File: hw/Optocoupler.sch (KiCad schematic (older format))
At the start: 10 parts, among them J1 Conn_01x02_Female, U2 EL357N(A)(TA)-G

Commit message: Add connectors
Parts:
- gave numbers to parts that had none: 6
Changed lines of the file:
@@
 $EndComp
 $Comp
-L Device:R R?
+L Device:R R7
 U 1 1 5F8C6DD6
 P 7100 2500
-F 0 "R?" H 7170 2546 50  0000 L CNN
+F 0 "R7" H 7170 2546 50  0000 L CNN
 F 1 "10k" H 7170 2455 50  0000 L CNN
 F 2 "" V 7030 2500 50  0001 C CNN
@@
 	7100 2950 7100 3050
 $Comp
-L power:GND #PWR?
+L power:GND #PWR0109
 U 1 1 5F8C950C
 P 7100 3050
-F 0 "#PWR?" H 7100 2800 50  0001 C CNN
+F 0 "#PWR0109" H 7100 2800 50  0001 C CNN
 F 1 "GND" H 7105 2877 50  0000 C CNN
 F 2 "" H 7100 3050 50  0001 C CNN
@@
 P 6300 4550
 AR Path="/5F8D198E" Ref="U?"  Part="1"
-AR Path="/5F8B0B95/5F8D198E" Ref="U?"  Part="1"
-F 0 "U?" H 6300 4920 50  0000 C CNN
+AR Path="/5F8B0B95/5F8D198E" Ref="U1"  Part="1"
+F 0 "U1" H 6300 4920 50  0000 C CNN
 F 1 "EL357N(A)(TA)-G" H 6300 4829 50  0000 C CNN
 F 2 "EL357N_A__TA_-G:SOP254P700X200-4N" H 6300 4550 50  0001 L BNN
@@
 $EndComp
 $Comp
-L Connector:Conn_01x02_Female J?
+L Connector:Conn_01x02_Female J2
 U 1 1 5F8D1994
 P 4100 4600
-F 0 "J?" H 3992 4275 50  0000 C CNN
+F 0 "J2" H 3992 4275 50  0000 C CNN
 F 1 "Conn_01x02_Female" H 3992 4366 50  0000 C CNN
 F 2 "" H 4100 4600 50  0001 C CNN
@@
 $EndComp
 $Comp
-L B5819W:B5819W D?
+L B5819W:B5819W D3
 U 1 1 5F8D199A
 P 5300 4550
-F 0 "D?" V 5346 4460 50  0000 R CNN
+F 0 "D3" V 5346 4460 50  0000 R CNN
 F 1 "B5819W" V 5255 4460 50  0000 R CNN
 F 2 "B5819W:B5819W_SOD-123" H 5300 4550 50  0001 L BNN
@@
 	4850 4500 5000 4500
 $Comp
-L Device:R R?
+L Device:R R6
 U 1 1 5F8D19AB
 P 4700 4500
-F 0 "R?" V 4493 4500 50  0000 C CNN
+F 0 "R6" V 4493 4500 50  0000 C CNN
 F 1 "20k" V 4584 4500 50  0000 C CNN
 F 2 "" V 4630 4500 50  0001 C CNN
@@
 $EndComp
 $Comp
-L Device:R R?
+L Device:R R8
 U 1 1 5F8D19B1
 P 7100 4200
-F 0 "R?" H 7170 4246 50  0000 L CNN
+F 0 "R8" H 7170 4246 50  0000 L CNN
 F 1 "10k" H 7170 4155 50  0000 L CNN
 F 2 "" V 7030 4200 50  0001 C CNN
@@
 	7100 4650 7100 4750
 $Comp
-L power:GND #PWR?
+L power:GND #PWR0110
 U 1 1 5F8D19BD
 P 7100 4750
-F 0 "#PWR?" H 7100 4500 50  0001 C CNN
+F 0 "#PWR0110" H 7100 4500 50  0001 C CNN
 F 1 "GND" H 7105 4577 50  0000 C CNN
 F 2 "" H 7100 4750 50  0001 C CNN
@@
 OPTO_STOP
 $Comp
-L power:+3V3 #PWR?
+L power:+3V3 #PWR0111
 U 1 1 5F8E1D5E
 P 7100 4050
-F 0 "#PWR?" H 7100 3900 50  0001 C CNN
+F 0 "#PWR0111" H 7100 3900 50  0001 C CNN
 F 1 "+3V3" H 7115 4223 50  0000 C CNN
 F 2 "" H 7100 4050 50  0001 C CNN
@@
 $EndComp
 $Comp
-L power:+3V3 #PWR?
+L power:+3V3 #PWR0112
 U 1 1 5F8E5015
 P 7100 2350
-F 0 "#PWR?" H 7100 2200 50  0001 C CNN
+F 0 "#PWR0112" H 7100 2200 50  0001 C CNN
 F 1 "+3V3" H 7115 2523 50  0000 C CNN
 F 2 "" H 7100 2350 50  0001 C CNN

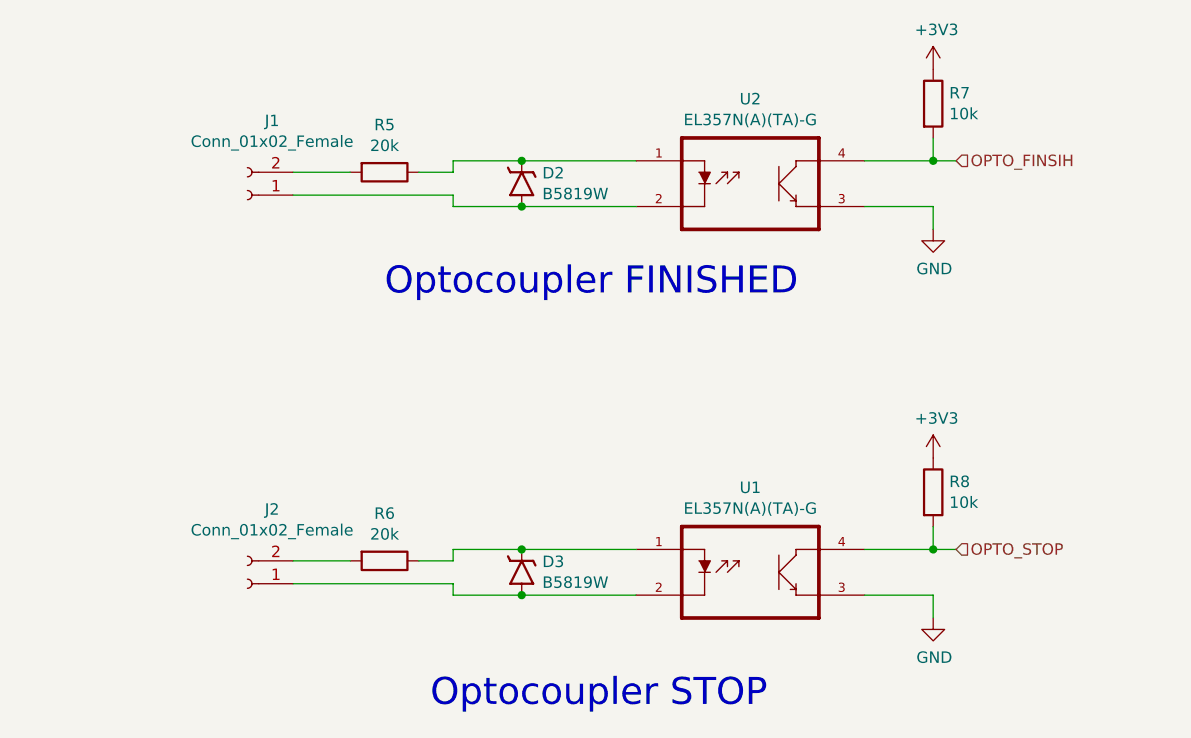
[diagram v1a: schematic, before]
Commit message: Update some packages, add 3D models
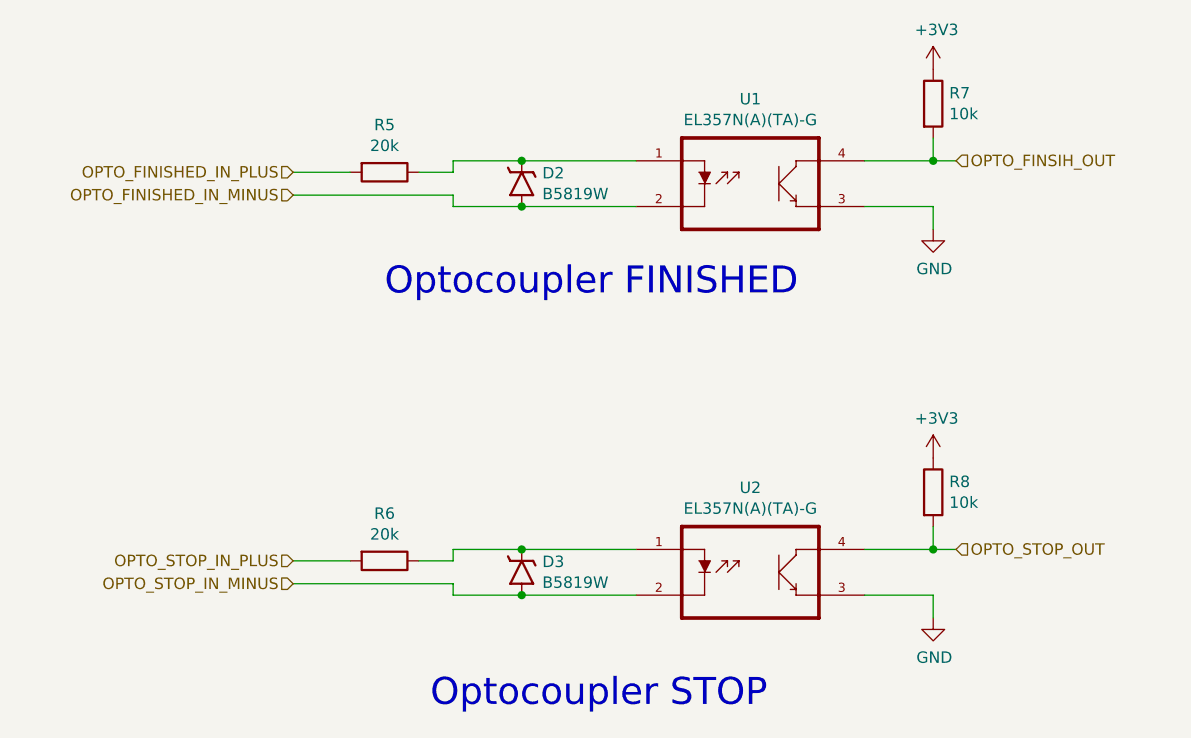
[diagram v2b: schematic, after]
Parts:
- removed J1, J2: Conn_01x02_Female, symbol Connector:Conn_01x02_Female
- D2, D3: LCSC_ID (none) -> C8598
- R5, R6: footprint (none) -> Resistor_SMD:R_0603_1608Metric; LCSC_ID (none) -> C4184
- R7, R8: footprint (none) -> Resistor_SMD:R_0603_1608Metric; LCSC_ID (none) -> C25804
- U1, U2: Field4 Good -> (none); Field5 EL357N_A__TA_-G -> (none); Field6 Optocoupler [Everlight Electronics] EL357N_A__TA_-G Optocou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 -> (none); Field7 IPC-7351B -> (none); Field8 0.10 USD -> (none); Field9 Everlight -> (none); LCSC_ID (none) -> C6649; Source (none) -> https://www.snapeda.com/parts/EL357N%28A%29%28TA%29-G/Everl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
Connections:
- net at D2.C, R5.1: now also U1.1; no longer U2.1
- net OPTO_FINISHED_IN_MINUS: now reaches D2.A
- net OPTO_FINISHED_IN_MINUS: now also U1.2; no longer U2.2
- net OPTO_FINISHED_IN_PLUS: now reaches R5.2
- net at D3.C, R6.1: now also U2.1; no longer U1.1
- net OPTO_STOP_IN_MINUS: now reaches D3.A
- net OPTO_STOP_IN_MINUS: now also U2.2; no longer U1.2
- net OPTO_STOP_IN_PLUS: now reaches R6.2
- net OPTO_FINSIH renamed OPTO_FINSIH_OUT
- net OPTO_FINSIH_OUT: now also U1.4; no longer U2.4
- net OPTO_STOP renamed OPTO_STOP_OUT
- net OPTO_STOP_OUT: now also U2.4; no longer U1.4
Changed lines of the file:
@@
 $EndDescr
-$Comp
-L EL357N_A__TA_-G:EL357N(A)(TA)-G U?
-U 1 1 5F8B3994
-P 6300 2850
-AR Path="/5F8B3994" Ref="U?"  Part="1"
-AR Path="/5F8B0B95/5F8B3994" Ref="U2"  Part="1"
-F 0 "U2" H 6300 3220 50  0000 C CNN
-F 1 "EL357N(A)(TA)-G" H 6300 3129 50  0000 C CNN
-F 2 "EL357N_A__TA_-G:SOP254P700X200-4N" H 6300 2850 50  0001 L BNN
-F 3 "SOP-4 Everlight" H 6300 2850 50  0001 L BNN
-F 4 "Good" H 6300 2850 50  0001 L BNN "Field4"
-F 5 "EL357N_A__TA_-G" H 6300 2850 50  0001 L BNN "Field5"
-F 6 "Optocoupler [Everlight Electronics] EL357N_A__TA_-G Optocoupler" H 6300 2850 50  0001 L BNN "Field6"
-F 7 "IPC-7351B" H 6300 2850 50  0001 L BNN "Field7"
-F 8 "0.10 USD" H 6300 2850 50  0001 L BNN "Field8"
-F 9 "Everlight" H 6300 2850 50  0001 L BNN "Field9"
-	1    6300 2850
-	1    0    0    -1
-$EndComp
-$Comp
-L Connector:Conn_01x02_Female J1
-U 1 1 5F8B4A8F
-P 4100 2900
-F 0 "J1" H 3992 2575 50  0000 C CNN
-F 1 "Conn_01x02_Female" H 3992 2666 50  0000 C CNN
-F 2 "" H 4100 2900 50  0001 C CNN
-F 3 "~" H 4100 2900 50  0001 C CNN
-	1    4100 2900
-	-1   0    0    1
-$EndComp
 $Comp
 L B5819W:B5819W D2
@@
 F 2 "B5819W:B5819W_SOD-123" H 5300 2850 50  0001 L BNN
 F 3 "" H 5300 2850 50  0001 C CNN
+F 4 "C8598" V 5300 2850 50  0001 C CNN "LCSC_ID"
 	1    5300 2850
 	0    -1   -1   0
@@
 F 0 "R5" V 4493 2800 50  0000 C CNN
 F 1 "20k" V 4584 2800 50  0000 C CNN
-F 2 "" V 4630 2800 50  0001 C CNN
+F 2 "Resistor_SMD:R_0603_1608Metric" V 4630 2800 50  0001 C CNN
 F 3 "~" H 4700 2800 50  0001 C CNN
+F 4 "C4184" V 4700 2800 50  0001 C CNN "LCSC_ID"
 	1    4700 2800
 	0    1    1    0
@@
 F 0 "R7" H 7170 2546 50  0000 L CNN
 F 1 "10k" H 7170 2455 50  0000 L CNN
-F 2 "" V 7030 2500 50  0001 C CNN
+F 2 "Resistor_SMD:R_0603_1608Metric" V 7008 2480 39  0001 C CNN
 F 3 "~" H 7100 2500 50  0001 C CNN
+F 4 "C25804" H 7100 2500 50  0001 C CNN "LCSC_ID"
 	1    7100 2500
 	1    0    0    -1
@@
 $EndComp
 Text HLabel 7200 2750 2    50   Input ~ 0
-OPTO_FINSIH
-$Comp
-L EL357N_A__TA_-G:EL357N(A)(TA)-G U?
-U 1 1 5F8D198E
-P 6300 4550
-AR Path="/5F8D198E" Ref="U?"  Part="1"
-AR Path="/5F8B0B95/5F8D198E" Ref="U1"  Part="1"
-F 0 "U1" H 6300 4920 50  0000 C CNN
-F 1 "EL357N(A)(TA)-G" H 6300 4829 50  0000 C CNN
-F 2 "EL357N_A__TA_-G:SOP254P700X200-4N" H 6300 4550 50  0001 L BNN
-F 3 "SOP-4 Everlight" H 6300 4550 50  0001 L BNN
-F 4 "Good" H 6300 4550 50  0001 L BNN "Field4"
-F 5 "EL357N_A__TA_-G" H 6300 4550 50  0001 L BNN "Field5"
-F 6 "Optocoupler [Everlight Electronics] EL357N_A__TA_-G Optocoupler" H 6300 4550 50  0001 L BNN "Field6"
-F 7 "IPC-7351B" H 6300 4550 50  0001 L BNN "Field7"
-F 8 "0.10 USD" H 6300 4550 50  0001 L BNN "Field8"
-F 9 "Everlight" H 6300 4550 50  0001 L BNN "Field9"
-	1    6300 4550
-	1    0    0    -1
-$EndComp
-$Comp
-L Connector:Conn_01x02_Female J2
-U 1 1 5F8D1994
-P 4100 4600
-F 0 "J2" H 3992 4275 50  0000 C CNN
-F 1 "Conn_01x02_Female" H 3992 4366 50  0000 C CNN
-F 2 "" H 4100 4600 50  0001 C CNN
-F 3 "~" H 4100 4600 50  0001 C CNN
-	1    4100 4600
-	-1   0    0    1
-$EndComp
+OPTO_FINSIH_OUT
 $Comp
 L B5819W:B5819W D3
@@
 F 2 "B5819W:B5819W_SOD-123" H 5300 4550 50  0001 L BNN
 F 3 "" H 5300 4550 50  0001 C CNN
+F 4 "C8598" V 5300 4550 50  0001 C CNN "LCSC_ID"
 	1    5300 4550
 	0    -1   -1   0
@@
 F 0 "R6" V 4493 4500 50  0000 C CNN
 F 1 "20k" V 4584 4500 50  0000 C CNN
-F 2 "" V 4630 4500 50  0001 C CNN
+F 2 "Resistor_SMD:R_0603_1608Metric" V 4630 4500 50  0001 C CNN
 F 3 "~" H 4700 4500 50  0001 C CNN
+F 4 "C4184" V 4700 4500 50  0001 C CNN "LCSC_ID"
 	1    4700 4500
 	0    1    1    0
@@
 F 0 "R8" H 7170 4246 50  0000 L CNN
 F 1 "10k" H 7170 4155 50  0000 L CNN
-F 2 "" V 7030 4200 50  0001 C CNN
+F 2 "Resistor_SMD:R_0603_1608Metric" V 7030 4200 50  0001 C CNN
 F 3 "~" H 7100 4200 50  0001 C CNN
+F 4 "C25804" H 7100 4200 50  0001 C CNN "LCSC_ID"
 	1    7100 4200
 	1    0    0    -1
@@
 $EndComp
 Text HLabel 7200 4450 2    50   Input ~ 0
-OPTO_STOP
+OPTO_STOP_OUT
 $Comp
 L power:+3V3 #PWR0111
@@
 Text Notes 4900 5150 0    118  ~ 0
 Optocoupler STOP
+Text HLabel 4300 4500 0    50   Input ~ 0
+OPTO_STOP_IN_PLUS
+Text HLabel 4300 4600 0    50   Input ~ 0
+OPTO_STOP_IN_MINUS
+Text HLabel 4300 2900 0    50   Input ~ 0
+OPTO_FINISHED_IN_MINUS
+Text HLabel 4300 2800 0    50   Input ~ 0
+OPTO_FINISHED_IN_PLUS
+$Comp
+L EL357N_A__TA_-G:EL357N(A)(TA)-G U2
+U 1 1 5F96692D
+P 6300 4550
+F 0 "U2" H 6300 4920 50  0000 C CNN
+F 1 "EL357N(A)(TA)-G" H 6300 4829 50  0000 C CNN
+F 2 "EL357N_A__TA_-G:SOP254P700X200-4N" H 5550 4150 50  0001 L BNN
+F 3 "https://www.snapeda.com/parts/EL357N(A)(TA)-G/Everlight%20Electronics/datasheet/" H 6300 4550 50  0001 L BNN
+F 4 "https://www.snapeda.com/parts/EL357N%28A%29%28TA%29-G/Everlight%20Electronics/view-part/?ref=search&t=EL357N(A)(TA)-G" H 6600 4000 50  0001 C CNN "Source"
+F 5 "C6649" H 6300 3850 50  0001 C CNN "LCSC_ID"
+	1    6300 4550
+	1    0    0    -1
+$EndComp
+$Comp
+L EL357N_A__TA_-G:EL357N(A)(TA)-G U1
+U 1 1 5F96CCB1
+P 6300 2850
+F 0 "U1" H 6300 3220 50  0000 C CNN
+F 1 "EL357N(A)(TA)-G" H 6300 3129 50  0000 C CNN
+F 2 "EL357N_A__TA_-G:SOP254P700X200-4N" H 5550 2450 50  0001 L BNN
+F 3 "https://www.snapeda.com/parts/EL357N(A)(TA)-G/Everlight%20Electronics/datasheet/" H 6300 2850 50  0001 L BNN
+F 4 "https://www.snapeda.com/parts/EL357N%28A%29%28TA%29-G/Everlight%20Electronics/view-part/?ref=search&t=EL357N(A)(TA)-G" H 6600 2300 50  0001 C CNN "Source"
+F 5 "C6649" H 6300 2150 50  0001 C CNN "LCSC_ID"
+	1    6300 2850
+	1    0    0    -1
+$EndComp
 $EndSCHEMATC

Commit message: Routing schema
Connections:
- net OPTO_FINSIH_OUT renamed OPTO_FINSIHED_OUT
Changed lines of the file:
@@
 $EndComp
 Text HLabel 7200 2750 2    50   Input ~ 0
-OPTO_FINSIH_OUT
+OPTO_FINSIHED_OUT
 $Comp
 L B5819W:B5819W D3
